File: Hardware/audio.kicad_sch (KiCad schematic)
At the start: 17 parts, among them J8 Conn_01x03, U4 LP5907MFX-3.3, U5 PCM5100

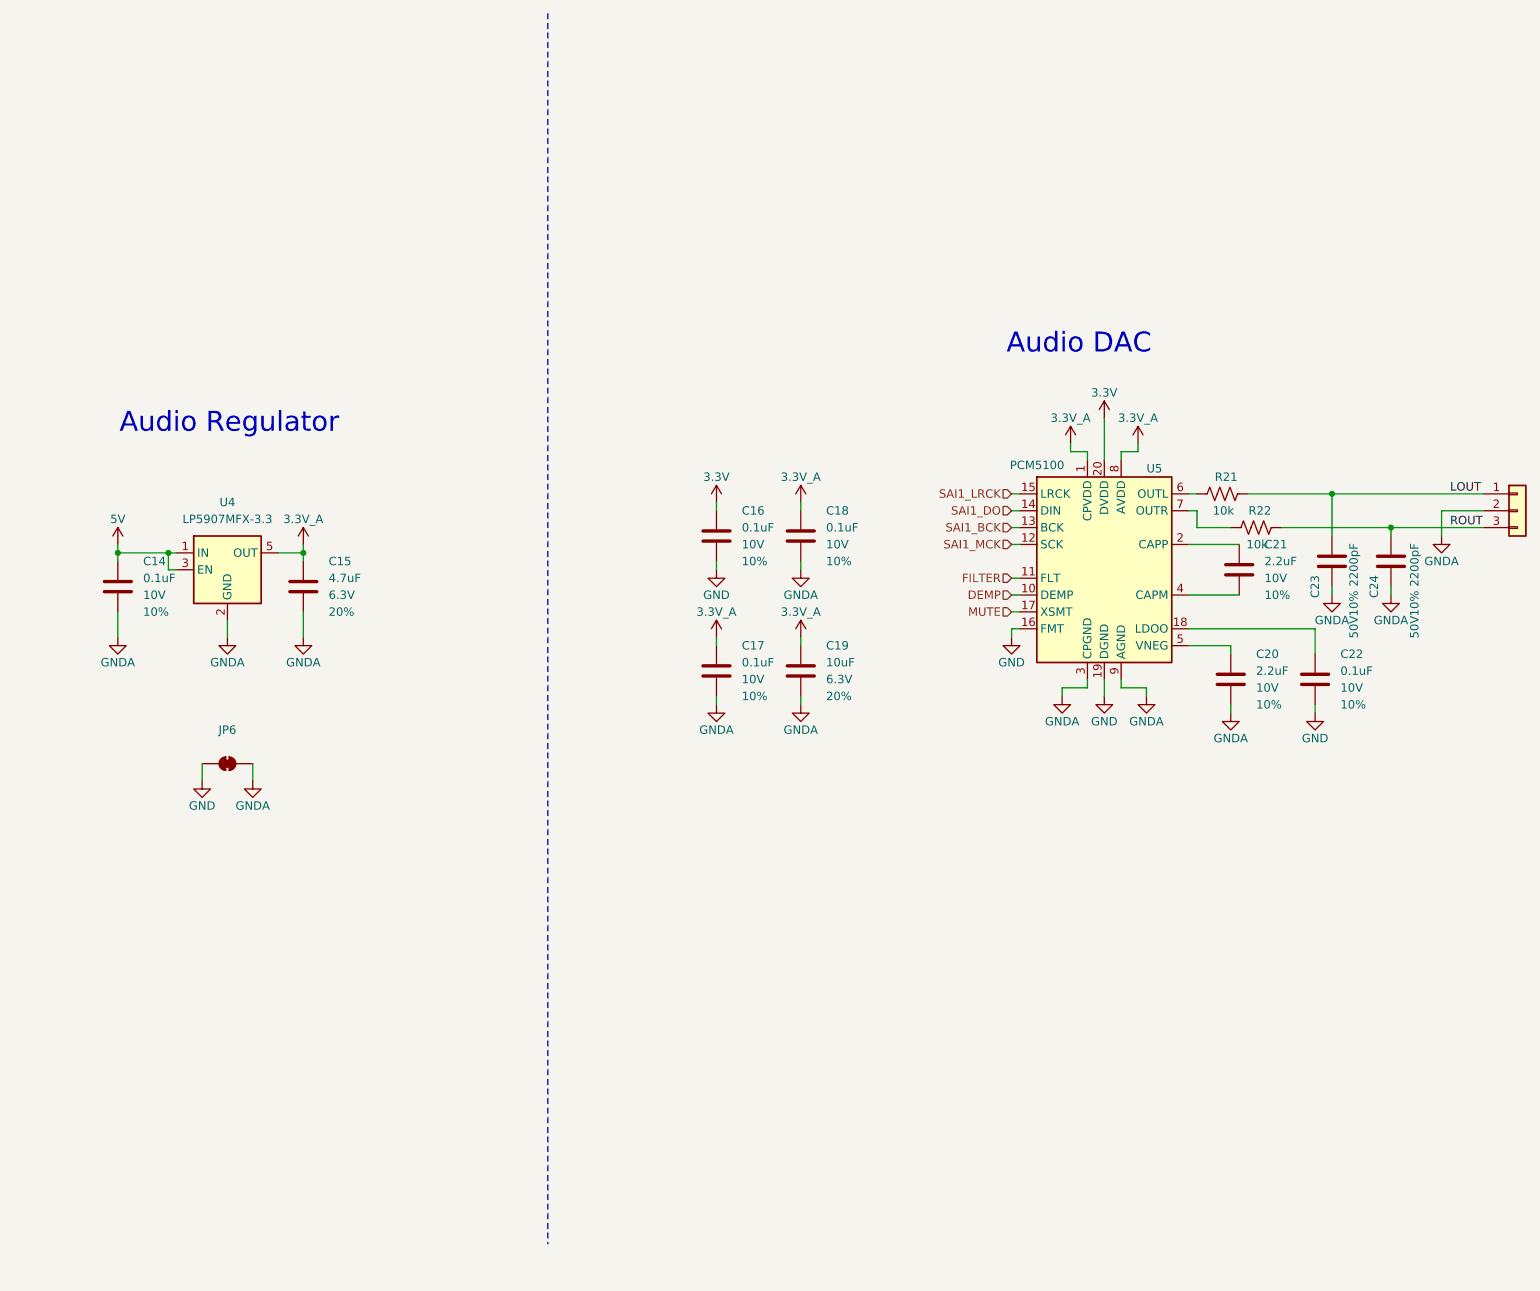
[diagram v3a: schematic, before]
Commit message: Moved all components to 25 mil grid. Rerouted accordingly. Updated 3D model colors.
Signed-off-by: Jamie Robertson <jrr@robertsonics.com>
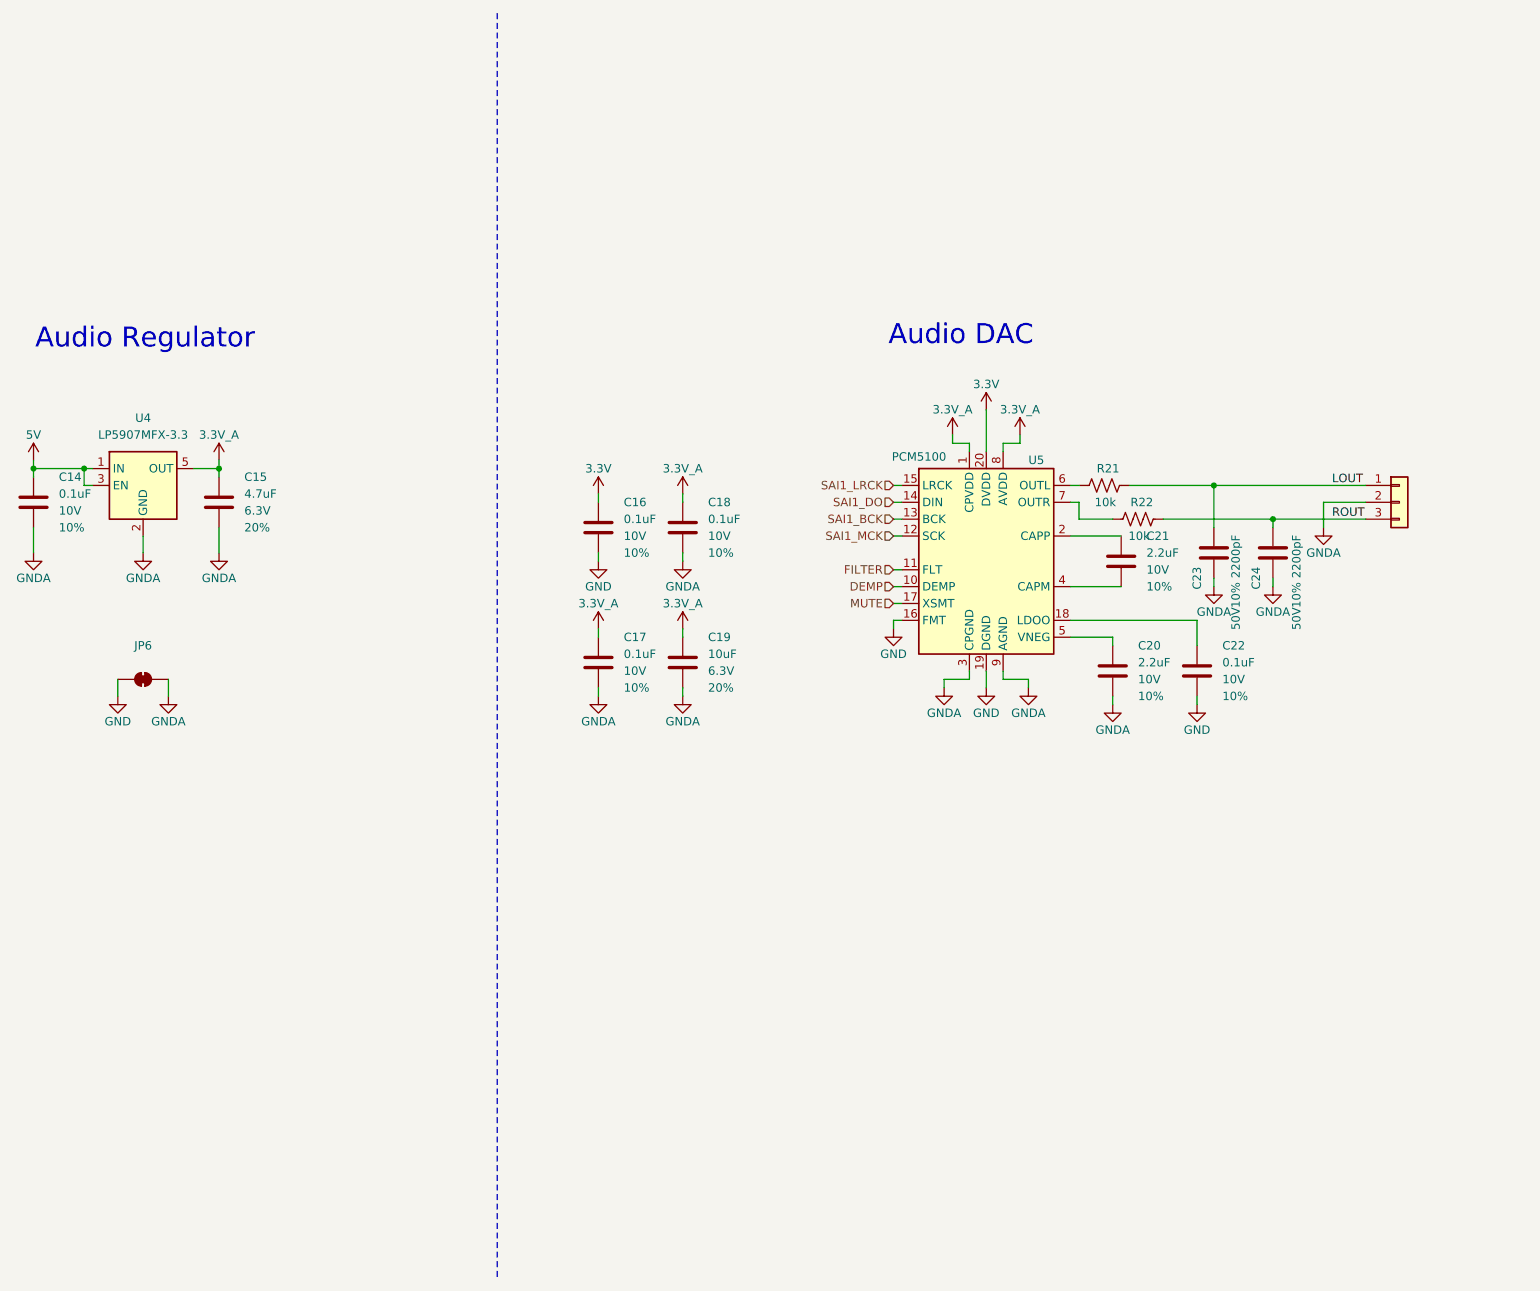
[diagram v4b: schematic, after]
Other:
- moved on the sheet: C14, C15, C16, C17, C18, C19, C20, C21, C22, C23, C24, JP6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

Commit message: Update product name to SparkFun Qwiic WAV Trigger Pro
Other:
- title: WAV Trigger Pro -> SparkFun Qwiic WAV Trigger Pro
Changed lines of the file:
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@@
 	(paper "A")
 	(title_block
-		(title "WAV Trigger Pro")
+		(title "SparkFun Qwiic WAV Trigger Pro")
 		(rev "1.0")
 		(company "Robertsonics / SparkFun")

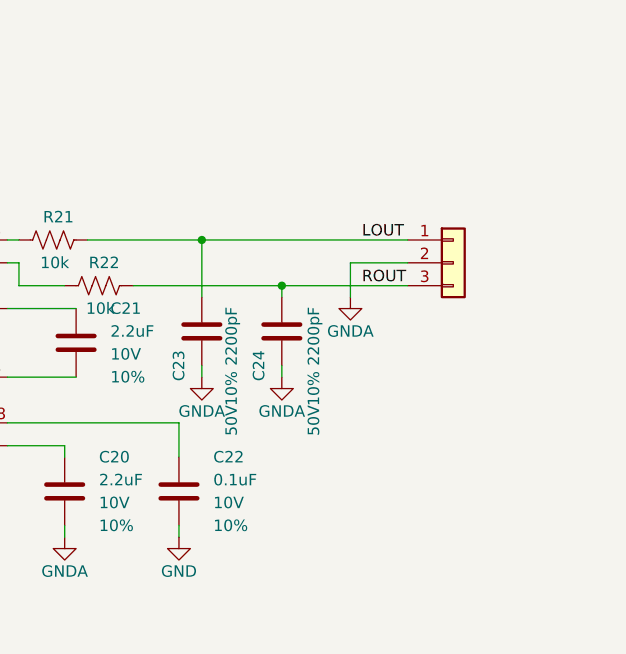
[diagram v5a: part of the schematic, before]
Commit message: Add 5V boost. Add 3.5mm jack.
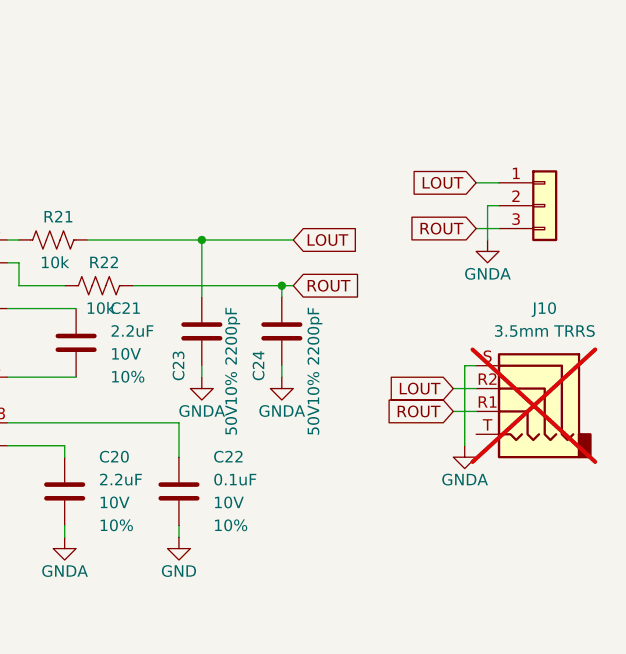
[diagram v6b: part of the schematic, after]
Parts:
- added J10: 3.5mm TRRS, SparkFun-Connector:Audio_Jack_3.5mm_TRRS_SMD_RA, symbol SparkFun-Connector:Audio Jack TRRS 3.5mm SMD
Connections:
- net GNDA: now also J10.S
- net LOUT: now also J10.R2
- net ROUT: now also J10.R1

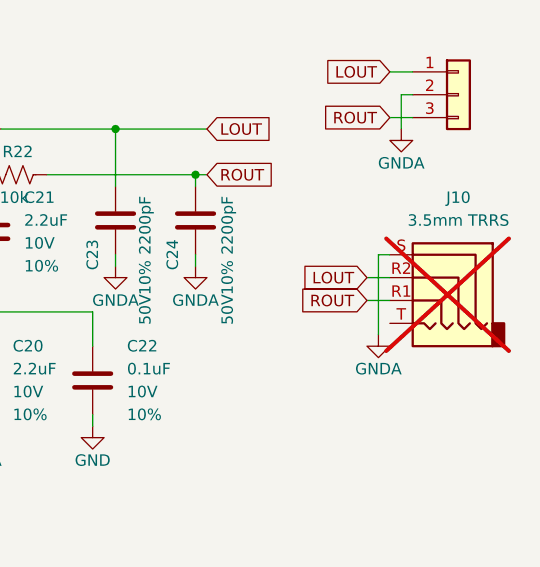
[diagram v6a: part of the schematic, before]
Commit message: Added boost converter to layout.
Signed-off-by: Jamie Robertson <jrr@robertsonics.com>
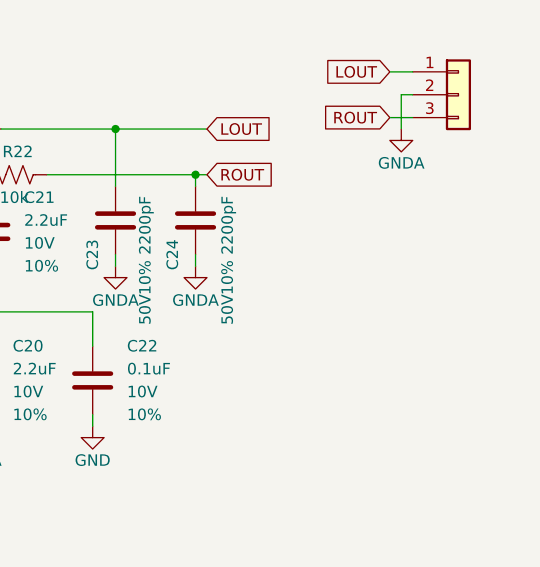
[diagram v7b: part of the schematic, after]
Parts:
- removed J10: 3.5mm TRRS, SparkFun-Connector:Audio_Jack_3.5mm_TRRS_SMD_RA, symbol SparkFun-Connector:Audio Jack TRRS 3.5mm SMD
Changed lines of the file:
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@@
-	(wire
-		(pts
-			(xy 245.11 100.33) (xy 247.65 100.33)
-		)
-		(stroke
-			(width 0)
-			(type default)
-		)
-	)
 	(wire
 		(pts
@@
 	(wire
 		(pts
-			(xy 245.11 102.87) (xy 247.65 102.87)
-		)
-		(stroke
-			(width 0)
-			(type default)
-		)
-	)
-	(wire
-		(pts
 			(xy 168.91 91.44) (xy 170.18 91.44)
 		)
@@
 	(wire
 		(pts
-			(xy 246.38 97.79) (xy 247.65 97.79)
-		)
-		(stroke
-			(width 0)
-			(type default)
-		)
-	)
-	(wire
-		(pts
 			(xy 209.55 88.9) (xy 226.06 88.9)
 		)
@@
 		(pts
 			(xy 124.46 95.25) (xy 124.46 93.98)
-		)
-		(stroke
-			(width 0)
-			(type default)
-		)
-	)
-	(wire
-		(pts
-			(xy 246.38 106.68) (xy 246.38 97.79)
 		)
 		(stroke
@@
 		(property "Intersheetrefs" "${INTERSHEET_REFS}"
 			(at 239.7662 82.55 0)
-			(effects
-				(font
-					(size 1.27 1.27)
-				)
-				(justify right)
-				(hide yes)
-			)
-		)
-	)
-	(global_label "ROUT"
-		(shape input)
-		(at 245.11 102.87 180)
-		(fields_autoplaced yes)
-		(effects
-			(font
-				(size 1.27 1.27)
-			)
-			(justify right)
-		)
-		(property "Intersheetrefs" "${INTERSHEET_REFS}"
-			(at 237.2262 102.87 0)
-			(effects
-				(font
-					(size 1.27 1.27)
-				)
-				(justify right)
-				(hide yes)
-			)
-		)
-	)
-	(global_label "LOUT"
-		(shape input)
-		(at 245.11 100.33 180)
-		(fields_autoplaced yes)
-		(effects
-			(font
-				(size 1.27 1.27)
-			)
-			(justify right)
-		)
-		(property "Intersheetrefs" "${INTERSHEET_REFS}"
-			(at 237.4681 100.33 0)
 			(effects
 				(font
@@
 				(path "/4c0b78e3-6801-43aa-85ca-70880324c2bd/79c75e5e-ffba-407e-9374-79e1c26e51a6"
 					(reference "C15")
-					(unit 1)
-				)
-			)
-		)
-	)
-	(symbol
-		(lib_id "power:GNDA")
-		(at 246.38 106.68 0)
-		(unit 1)
-		(exclude_from_sim no)
-		(in_bom yes)
-		(on_board yes)
-		(dnp no)
-		(property "Reference" "#PWR090"
-			(at 246.38 113.03 0)
-			(effects
-				(font
-					(size 1.27 1.27)
-				)
-				(hide yes)
-			)
-		)
-		(property "Value" "GNDA"
-			(at 246.38 110.49 0)
-			(effects
-				(font
-					(size 1.27 1.27)
-				)
-			)
-		)
-		(property "Footprint" ""
-			(at 246.38 106.68 0)
-			(effects
-				(font
-					(size 1.27 1.27)
-				)
-				(hide yes)
-			)
-		)
-		(property "Datasheet" ""
-			(at 246.38 106.68 0)
-			(effects
-				(font
-					(size 1.27 1.27)
-				)
-				(hide yes)
-			)
-		)
-		(property "Description" "Power symbol creates a global label with name \"GNDA\" , analog ground"
-			(at 246.38 106.68 0)
-			(effects
-				(font
-					(size 1.27 1.27)
-				)
-				(hide yes)
-			)
-		)
-		(pin "1"
-		)
-		(instances
-			(project "SparkFun_Qwiic_Turntable"
-				(path "/4c0b78e3-6801-43aa-85ca-70880324c2bd/79c75e5e-ffba-407e-9374-79e1c26e51a6"
-					(reference "#PWR090")
 					(unit 1)
 				)
@@
 					(unit 1)
 				)
-			)
-		)
-	)
-	(symbol
-		(lib_id "SparkFun-Connector:Audio Jack TRRS 3.5mm SMD")
-		(at 252.73 100.33 0)
-		(mirror y)
-		(unit 1)
-		(exclude_from_sim no)
-		(in_bom yes)
-		(on_board yes)
-		(dnp yes)
-		(property "Reference" "J10"
-			(at 255.27 91.44 0)
-			(effects
-				(font
-					(size 1.27 1.27)
-				)
-			)
-		)
-		(property "Value" "3.5mm TRRS"
-			(at 255.27 93.98 0)
-			(effects
-				(font
-					(size 1.27 1.27)
-				)
-			)
-		)
-		(property "Footprint" "SparkFun-Connector:Audio_Jack_3.5mm_TRRS_SMD_RA"
-			(at 252.73 111.76 0)
-			(effects
-				(font
-					(size 1.27 1.27)
-				)
-				(hide yes)
-			)
-		)
-		(property "Datasheet" "https://cdn.sparkfun.com/datasheets/Prototyping/20153.pdf"
-			(at 252.73 109.22 0)
-			(effects
-				(font
-					(size 1.27 1.27)
-				)
-				(hide yes)
-			)
-		)
-		(property "Description" "Audio Jack, 4 Poles (TRRS)"
-			(at 252.73 114.3 0)
-			(effects
-				(font
-					(size 1.27 1.27)
-				)
-				(hide yes)
-			)
-		)
-		(property "PROD-ID" "CONN-10676"
-			(at 252.73 116.84 0)
-			(effects
-				(font
-					(size 1.27 1.27)
-				)
-				(hide yes)
-			)
-		)
-		(pin "R1"
-		)
-		(pin "T"
-		)
-		(pin "S"
-		)
-		(pin "R2"
-		)
-		(instances
-			(project "SparkFun_Qwiic_Turntable"
-				(path "/4c0b78e3-6801-43aa-85ca-70880324c2bd/79c75e5e-ffba-407e-9374-79e1c26e51a6"
-					(reference "J10")
-					(unit 1)
-				)
